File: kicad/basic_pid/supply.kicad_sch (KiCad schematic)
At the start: 60 parts, among them J5 Screw_Terminal_01x04, J6 Screw_Terminal_01x03, SW1 SW_DPDT_x2, SW10 SW_DPDT_x2, SW2 SW_DPDT_x2, SW3 SW_DPDT_x2, SW5 SW_DPDT_x2, U14 LM2940CS-12/NOPB, U15 LM2990SX-12, U16 LM317_TO-252

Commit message: Fixed wrong part and added shunt resistor values
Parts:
- RV7: DIGIKEY 3296Y-202LF-ND -> SP064W-2.0K-ND; PARTNO 3296Y-1-202LF -> M64W202KB40
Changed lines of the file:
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@@
       (effects (font (size 1.27 1.27)) hide)
     )
-    (property "PARTNO" "3296Y-1-202LF" (at 223.52 100.965 0)
+    (property "PARTNO" "M64W202KB40" (at 223.52 100.965 0)
       (effects (font (size 1.27 1.27)) hide)
     )
-    (property "DIGIKEY" "3296Y-202LF-ND" (at 223.52 100.965 0)
+    (property "DIGIKEY" "SP064W-2.0K-ND" (at 223.52 100.965 0)
       (effects (font (size 1.27 1.27)) hide)
     )

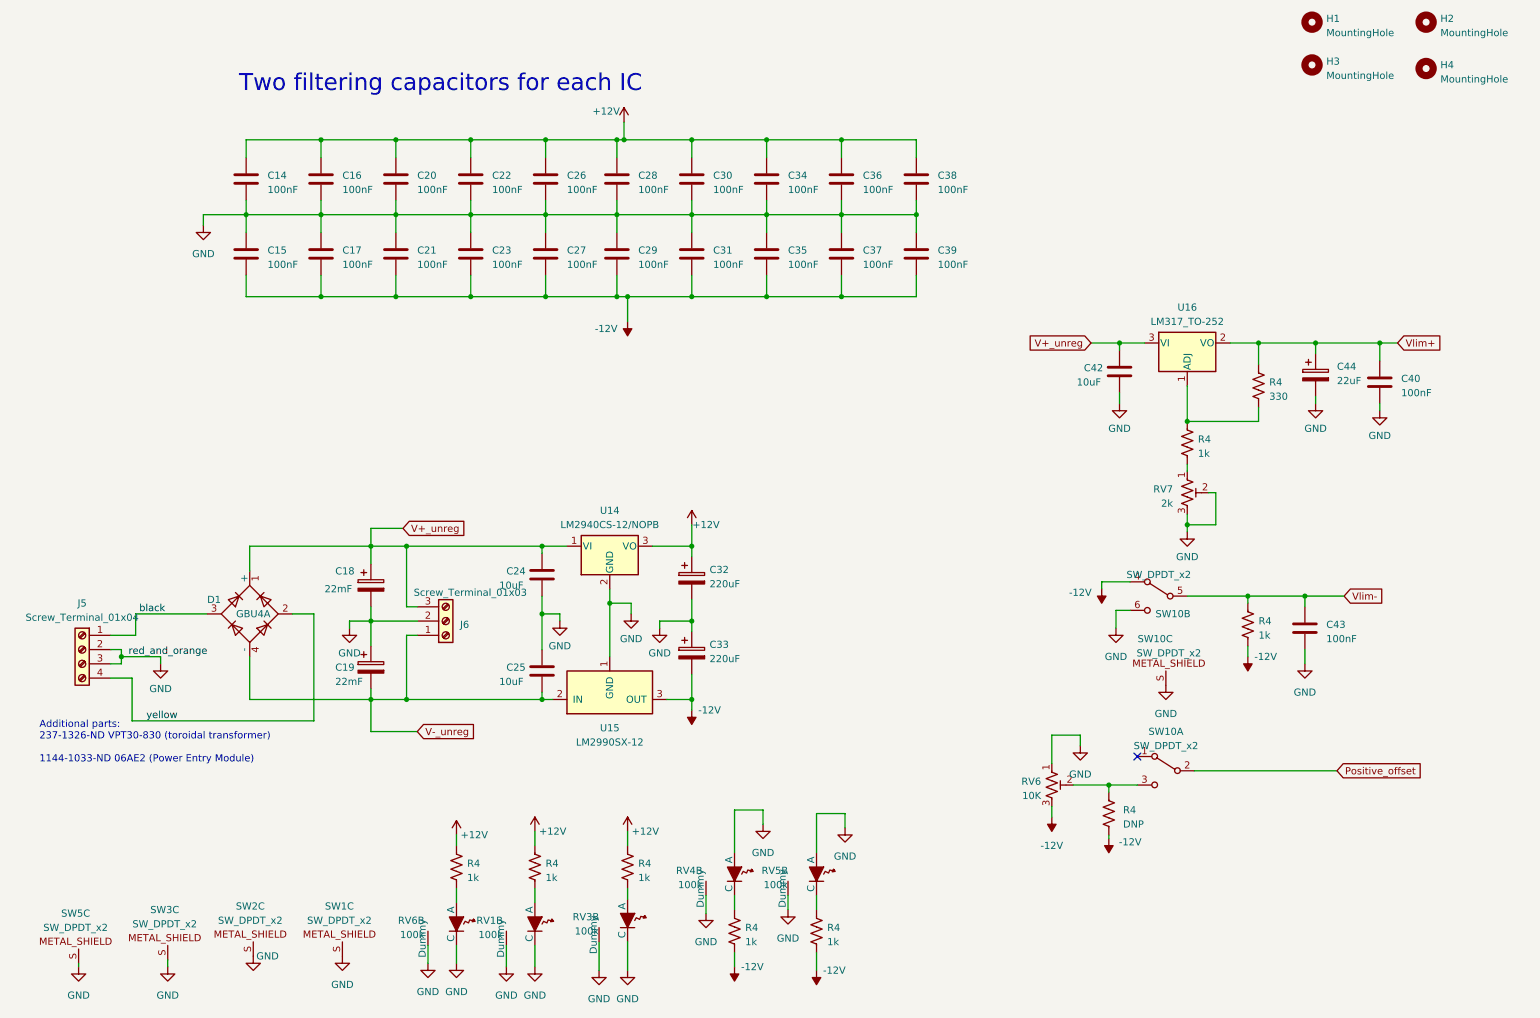
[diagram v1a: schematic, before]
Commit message: Fixed monitor instability
Added a 3.3 kOhm resistor on each output buffer's bandwith control pin
to increase the bandwidth from 30 MHz to 90 MHz.
This should prevent oscillations and instabilities we noticed while
testing the PID
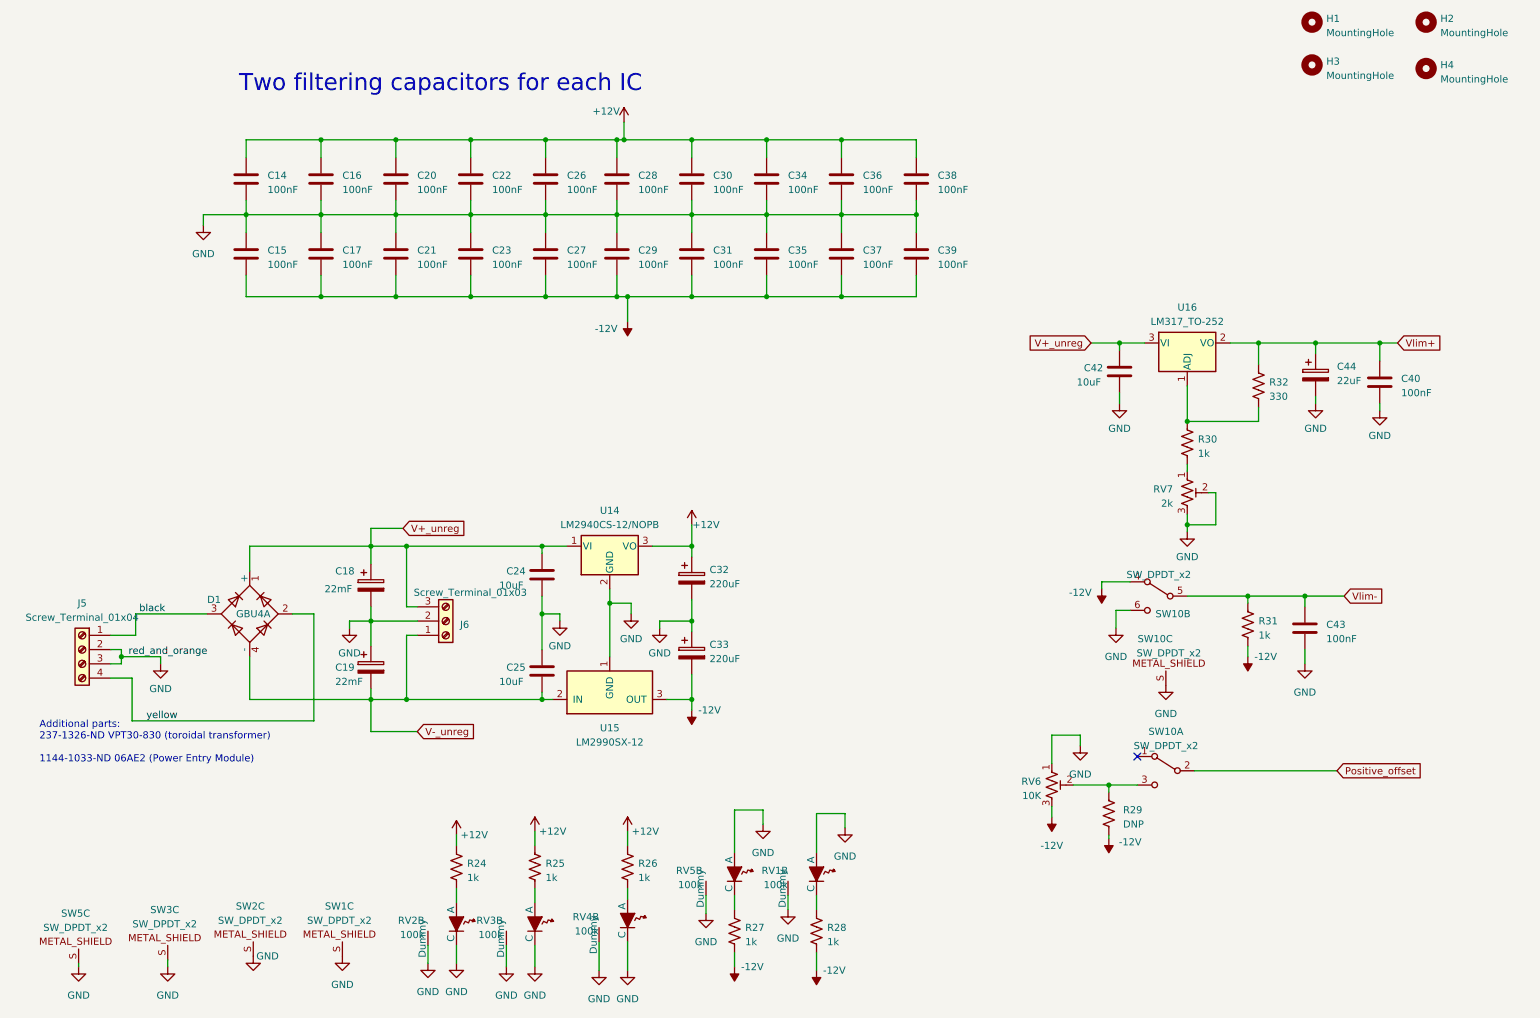
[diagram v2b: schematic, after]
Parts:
- renumbered R4 to R24, R4 to R25, R4 to R26, R4 to R27, R4 to R28, R4 to R29, R4 to R30, R4 to R31, R4 to R32, RV5 to RV1, RV6 to RV2, RV1 to RV3, RV3 to RV4, RV4 to RV5

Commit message: Not sure if it works: Just a possibile fix for a noisy monitor when sampling error signal
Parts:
- C18, C19: MPN (none) -> 380LX223M035K052
- C32, C33: MPN (none) -> EEE-1VA221UP
- C44: MPN (none) -> UCM1V220MCL1GS
- D1: MPN (none) -> GBU4A
- RV1, RV2, RV3, RV4, RV5: MPN (none) -> PTL45-15O0-104B1
- RV6: MPN (none) -> 3296W-1-103RLF
- RV7: MPN (none) -> M64W202KB40
- SW1, SW10, SW2, SW3, SW5: MPN (none) -> 1825289-1
- U14: MPN (none) -> LM2940CS-12/NOPB
- U15: MPN (none) -> LM2990SX-12/NOPB
- U16: MPN (none) -> LM317MDT-TR
